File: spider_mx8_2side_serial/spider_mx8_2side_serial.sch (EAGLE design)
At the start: 8 parts, among them J1 AVR_SPI_PRG_6NS

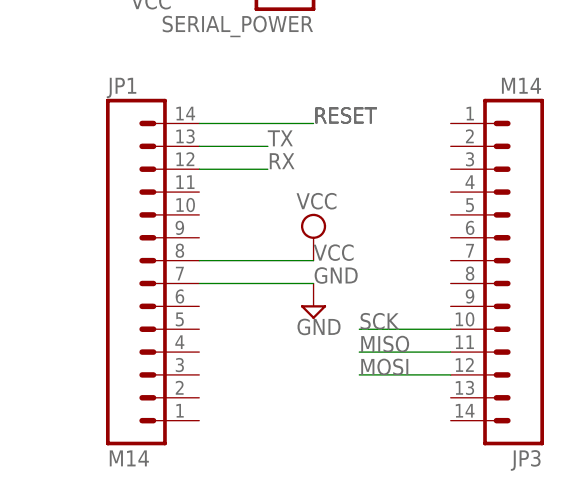
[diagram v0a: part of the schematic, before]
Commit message: cleanup -- renaming to match website
and deleting the stuff I don't use
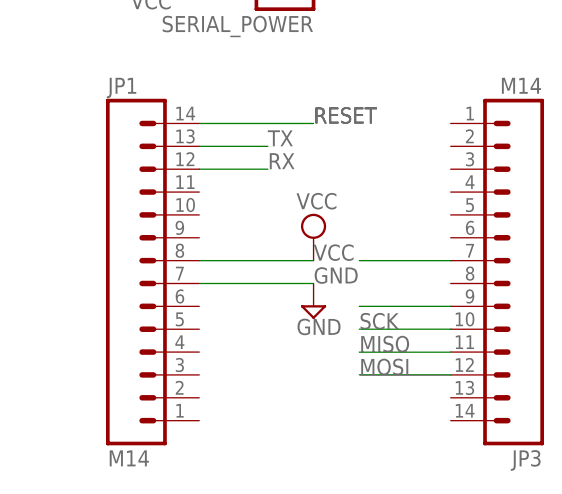
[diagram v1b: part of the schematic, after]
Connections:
- net GND: now also JP3.7
- net VCC: now also JP3.9
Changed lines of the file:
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@@
 <pinref part="SERIAL_POWER" gate="G$1" pin="2"/>
+</segment>
+<segment>
+<pinref part="JP3" gate="G$1" pin="9"/>
+<wire x1="83.82" y1="-7.62" x2="73.66" y2="-7.62" width="0.1524" layer="91"/>
 </segment>
 </net>
@@
 <pinref part="JP2" gate="G$1" pin="GND"/>
 </segment>
+<segment>
+<pinref part="JP3" gate="G$1" pin="7"/>
+<wire x1="83.82" y1="-2.54" x2="73.66" y2="-2.54" width="0.1524" layer="91"/>
+</segment>
 </net>
